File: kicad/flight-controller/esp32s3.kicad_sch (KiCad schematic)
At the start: 15 parts, among them J13 USB-C, SW1 TS-1088, SW2 TS-1088, U1 ESP32-S3-WROOM-1

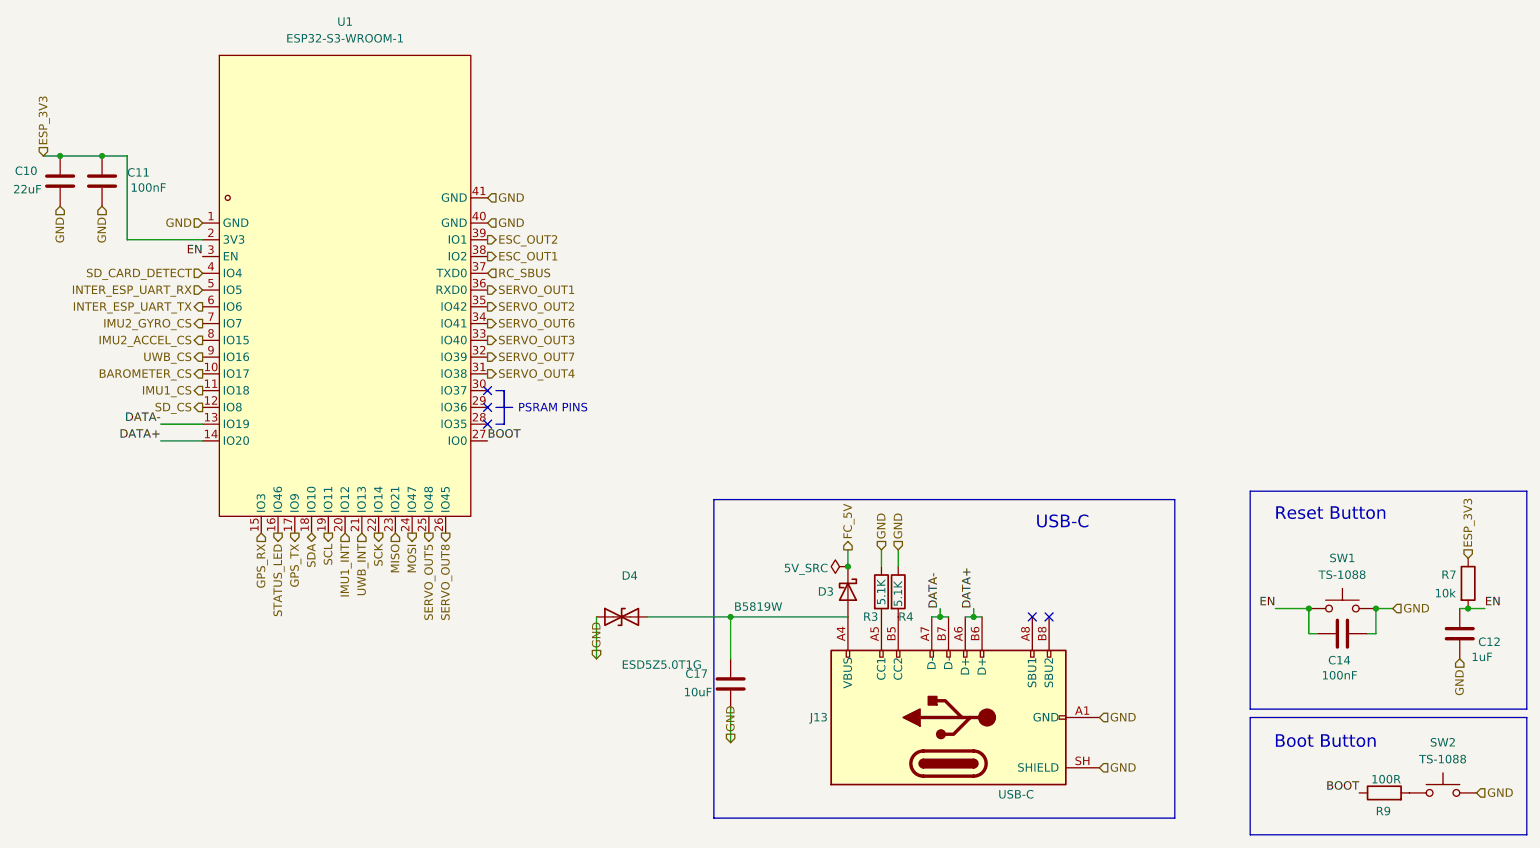
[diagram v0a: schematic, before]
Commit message: removed basestation code and v3.1 of fc pcb
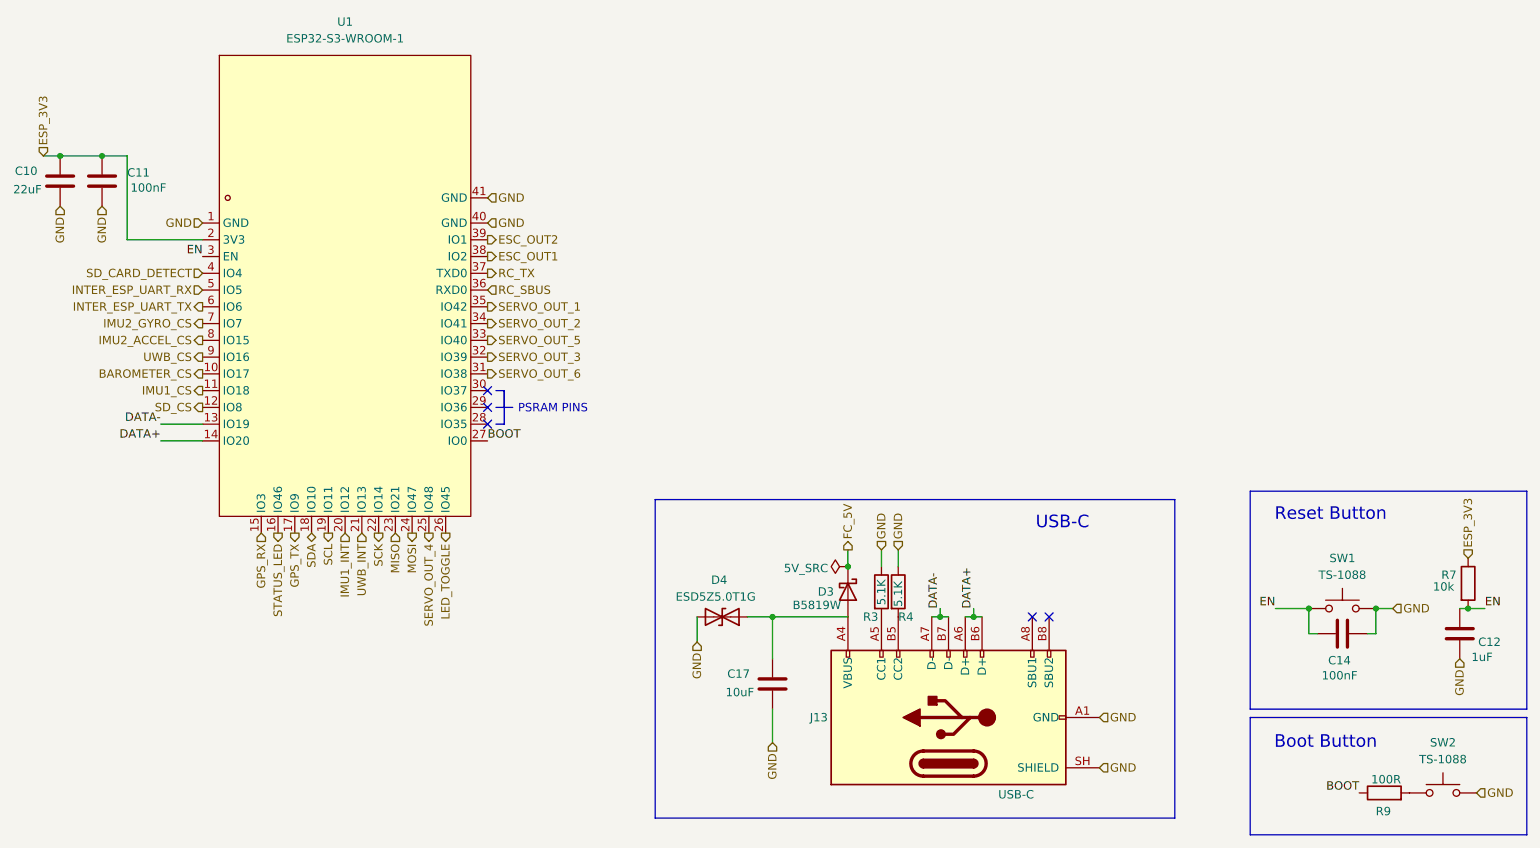
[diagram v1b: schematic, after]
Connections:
- net SERVO_OUT1 is gone; now on net RC_SBUS: U1.36 (RXD0)
- net GND: now also D4.2 (A2); no longer D4.1 (A1)
- net RC_SBUS: no longer U1.37 (TXD0)
- net at C17.1, D3.2 (A), J13.A4 (VBUS)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: now also D4.1 (A1); no longer D4.2 (A2)
- net SERVO_OUT2 renamed SERVO_OUT_1
- net SERVO_OUT3 renamed SERVO_OUT_5
- net SERVO_OUT4 renamed SERVO_OUT_6
- net SERVO_OUT5 renamed SERVO_OUT_4
- net SERVO_OUT6 renamed SERVO_OUT_2
- net SERVO_OUT7 renamed SERVO_OUT_3
- net SERVO_OUT8 renamed LED_TOGGLE
- new net RC_TX: U1.37 (TXD0)
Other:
- moved on the sheet: C17, D4
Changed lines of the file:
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@@
 	)
 	(rectangle
-		(start 152.4 100.33)
+		(start 143.51 100.33)
 		(end 222.25 148.59)
 		(stroke
@@
 	)
 	(junction
-		(at 154.94 118.11)
-		(diameter 0)
-		(color 0 0 0 0)
-	)
-	(junction
 		(at 172.72 110.49)
 		(diameter 0)
@@
 	)
 	(junction
+		(at 161.29 118.11)
+		(diameter 0)
+		(color 0 0 0 0)
+	)
+	(junction
 		(at 186.69 118.11)
 		(diameter 0)
@@
 	(wire
 		(pts
-			(xy 134.62 118.11) (xy 134.62 124.46)
+			(xy 149.86 118.11) (xy 149.86 121.92)
 		)
 		(stroke
@@
 	(wire
 		(pts
-			(xy 172.72 118.11) (xy 154.94 118.11)
+			(xy 172.72 118.11) (xy 161.29 118.11)
 		)
 		(stroke
@@
 	(wire
 		(pts
-			(xy 154.94 124.46) (xy 154.94 118.11)
+			(xy 161.29 124.46) (xy 161.29 118.11)
 		)
 		(stroke
@@
 	(wire
 		(pts
-			(xy 154.94 132.08) (xy 154.94 137.16)
+			(xy 161.29 132.08) (xy 161.29 137.16)
 		)
 		(stroke
@@
 	(wire
 		(pts
-			(xy 154.94 118.11) (xy 142.24 118.11)
+			(xy 157.48 118.11) (xy 161.29 118.11)
 		)
 		(stroke
@@
 			)
 			(justify left bottom)
+		)
+	)
+	(hierarchical_label "LED_TOGGLE"
+		(shape output)
+		(at 111.76 105.41 270)
+		(effects
+			(font
+				(size 1.27 1.27)
+			)
+			(justify right)
 		)
 	)
@@
 		)
 	)
-	(hierarchical_label "SERVO_OUT7"
-		(shape output)
-		(at 118.11 78.74 0)
-		(effects
-			(font
-				(size 1.27 1.27)
-			)
-			(justify left)
-		)
-	)
 	(hierarchical_label "UWB_CS"
 		(shape output)
@@
 	(hierarchical_label "RC_SBUS"
 		(shape input)
-		(at 118.11 66.04 0)
-		(effects
-			(font
-				(size 1.27 1.27)
-			)
-			(justify left)
-		)
-	)
-	(hierarchical_label "SERVO_OUT3"
-		(shape output)
-		(at 118.11 76.2 0)
+		(at 118.11 68.58 0)
 		(effects
 			(font
@@
 		)
 	)
+	(hierarchical_label "SERVO_OUT_2"
+		(shape output)
+		(at 118.11 73.66 0)
+		(effects
+			(font
+				(size 1.27 1.27)
+			)
+			(justify left)
+		)
+	)
 	(hierarchical_label "INTER_ESP_UART_RX"
 		(shape input)
@@
 		)
 	)
-	(hierarchical_label "SERVO_OUT4"
+	(hierarchical_label "SERVO_OUT_3"
 		(shape output)
-		(at 118.11 81.28 0)
+		(at 118.11 78.74 0)
 		(effects
 			(font
@@
 		)
 	)
-	(hierarchical_label "SERVO_OUT1"
+	(hierarchical_label "SERVO_OUT_4"
 		(shape output)
-		(at 118.11 68.58 0)
-		(effects
-			(font
-				(size 1.27 1.27)
-			)
-			(justify left)
+		(at 109.22 105.41 270)
+		(effects
+			(font
+				(size 1.27 1.27)
+			)
+			(justify right)
 		)
 	)
@@
 		)
 	)
-	(hierarchical_label "SERVO_OUT2"
-		(shape output)
-		(at 118.11 71.12 0)
-		(effects
-			(font
-				(size 1.27 1.27)
-			)
-			(justify left)
-		)
-	)
 	(hierarchical_label "INTER_ESP_UART_TX"
 		(shape output)
@@
 		)
 	)
+	(hierarchical_label "RC_TX"
+		(shape output)
+		(at 118.11 66.04 0)
+		(effects
+			(font
+				(size 1.27 1.27)
+			)
+			(justify left)
+		)
+	)
 	(hierarchical_label "GND"
 		(shape input)
@@
 	(hierarchical_label "GND"
 		(shape input)
-		(at 154.94 137.16 90)
-		(effects
-			(font
-				(size 1.27 1.27)
-			)
-			(justify left)
+		(at 161.29 137.16 270)
+		(effects
+			(font
+				(size 1.27 1.27)
+			)
+			(justify right)
 		)
 	)
@@
 		)
 	)
-	(hierarchical_label "SERVO_OUT6"
-		(shape output)
-		(at 118.11 73.66 0)
-		(effects
-			(font
-				(size 1.27 1.27)
-			)
-			(justify left)
-		)
-	)
 	(hierarchical_label "GPS_RX"
 		(shape input)
@@
 		)
 	)
-	(hierarchical_label "SERVO_OUT8"
-		(shape output)
-		(at 111.76 105.41 270)
-		(effects
-			(font
-				(size 1.27 1.27)
-			)
-			(justify right)
-		)
-	)
 	(hierarchical_label "ESP_3V3"
 		(shape input)
@@
 		)
 	)
-	(hierarchical_label "SERVO_OUT5"
+	(hierarchical_label "SERVO_OUT_5"
 		(shape output)
-		(at 109.22 105.41 270)
-		(effects
-			(font
-				(size 1.27 1.27)
-			)
-			(justify right)
+		(at 118.11 76.2 0)
+		(effects
+			(font
+				(size 1.27 1.27)
+			)
+			(justify left)
+		)
+	)
+	(hierarchical_label "SERVO_OUT_1"
+		(shape output)
+		(at 118.11 71.12 0)
+		(effects
+			(font
+				(size 1.27 1.27)
+			)
+			(justify left)
 		)
 	)
 	(hierarchical_label "GND"
 		(shape input)
-		(at 134.62 124.46 90)
-		(effects
-			(font
-				(size 1.27 1.27)
-			)
-			(justify left)
+		(at 149.86 121.92 270)
+		(effects
+			(font
+				(size 1.27 1.27)
+			)
+			(justify right)
 		)
 	)
@@
 		(shape output)
 		(at 118.11 63.5 0)
+		(effects
+			(font
+				(size 1.27 1.27)
+			)
+			(justify left)
+		)
+	)
+	(hierarchical_label "SERVO_OUT_6"
+		(shape output)
+		(at 118.11 81.28 0)
 		(effects
 			(font
@@
 	(symbol
 		(lib_id "Device:D_TVS")
-		(at 138.43 118.11 0)
+		(at 153.67 118.11 180)
 		(unit 1)
 		(body_style 1)
@@
 		(dnp no)
 		(property "Reference" "D4"
-			(at 138.43 111.89 0)
+			(at 154.432 112.522 0)
 			(show_name no)
 			(do_not_autoplace no)
@@
 		)
 		(property "Value" "ESD5Z5.0T1G"
-			(at 138.43 125.38 0)
+			(at 158.75 115.062 0)
 			(show_name no)
 			(do_not_autoplace no)
@@
 		)
 		(property "Footprint" "Diode_SMD:D_SOD-523"
-			(at 138.43 118.11 0)
+			(at 153.67 118.11 0)
 			(hide yes)
 			(show_name no)
@@
 		)
 		(property "Datasheet" "https://www.lcsc.com/datasheet/C82044.pdf"
-			(at 138.43 118.11 0)
+			(at 153.67 118.11 0)
 			(hide yes)
 			(show_name no)
@@
 		)
 		(property "Description" "TVS diode, onsemi, 5V standoff / 6.2V breakdown, unidirectional"
-			(at 138.43 118.11 0)
+			(at 153.67 118.11 0)
 			(hide yes)
 			(show_name no)
@@
 		)
 		(property "Notes" "USB VBUS ESD/surge protection (added in review)"
-			(at 138.43 118.11 0)
+			(at 153.67 118.11 0)
 			(hide yes)
 			(show_name no)
@@
 		)
 		(property "LCSC Part" "C82044"
-			(at 138.43 118.11 0)
+			(at 153.67 118.11 0)
 			(hide yes)
 			(show_name no)
@@
 		)
 		(property "Value" "10k"
-			(at 261.62 114.554 0)
+			(at 261.366 113.538 0)
 			(show_name no)
 			(do_not_autoplace no)
@@
 	(symbol
 		(lib_id "Device:C")
-		(at 154.94 128.27 0)
+		(at 161.29 128.27 0)
 		(unit 1)
 		(body_style 1)
@@
 		(dnp no)
 		(property "Reference" "C17"
-			(at 148.086 126.746 0)
+			(at 154.436 126.746 0)
 			(show_name no)
 			(do_not_autoplace no)
@@
 		)
 		(property "Value" "10uF"
-			(at 147.832 129.54 0)
+			(at 154.182 129.54 0)
 			(show_name no)
 			(do_not_autoplace no)
@@
 		)
 		(property "Footprint" "Capacitor_SMD:C_0805_2012Metric"
-			(at 154.94 128.27 0)
+			(at 161.29 128.27 0)
 			(hide yes)
 			(show_name no)
@@
 		)
 		(property "Datasheet" "https://www.lcsc.com/datasheet/C440198.pdf"
-			(at 154.94 128.27 0)
+			(at 161.29 128.27 0)
 			(hide yes)
 			(show_name no)
@@
 		)
 		(property "Description" "Unpolarized capacitor, Murata GRM21BR61H106KE43L, 50V X5R"
-			(at 154.94 128.27 0)
+			(at 161.29 128.27 0)
 			(hide yes)
 			(show_name no)
@@
 		)
 		(property "Notes" "USB VBUS bulk/decoupling cap (added in review)"
-			(at 154.94 128.27 0)
+			(at 161.29 128.27 0)
 			(hide yes)
 			(show_name no)
@@
 		)
 		(property "LCSC Part" "C440198"
-			(at 154.94 128.27 0)
+			(at 161.29 128.27 0)
 			(hide yes)
 			(show_name no)
@@
 		)
 		(property "Value" "B5819W"
-			(at 155.448 116.586 90)
-			(show_name no)
-			(do_not_autoplace no)
+			(at 164.338 116.332 90)
+			(show_name no)
+			(do_not_autoplace no)

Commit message: pcb progress
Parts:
- added D8, D9: ESD5Z5.0T1G, Diode_SMD:D_SOD-523, symbol Device:D_TVS
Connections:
- net DATA+: now also D8.1 (A1)
- net DATA-: now also D9.1 (A1)
- net GND: now also D8.2 (A2), D9.2 (A2)

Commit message: Kicad FC v3.1 complete, Mission Controller and UWB boards v1 complete, firmware v2 complete!
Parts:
- removed D8, D9: ESD5Z5.0T1G, Diode_SMD:D_SOD-523, symbol Device:D_TVS
- added U5: USBLC6-2SC6, Package_TO_SOT_SMD:SOT-23-6, symbol Power_Protection:USBLC6-2SC6
- U1: LCSC Part C2913202 -> C2913205; MPN ESP32-S3-WROOM-1-N16R8 -> ESP32-S3-WROOM-1-N16R2
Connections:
- net DATA+: now also U5.1 (I/O1), U5.6 (I/O1)
- net DATA-: now also U5.3 (I/O2), U5.4 (I/O2)
- net GND: now also U5.2 (GND)
- net SD_CS: now also U1.30 (IO37); no longer U1.12 (IO8)
- net USB_VBUS: now reaches C17.1, D3.2 (A), D4.1 (A1), J13.A4 (VBUS), J13.A9 (VBUS), J13.B4 (VBUS), J13.B9 (VBUS)
- net USB_VBUS: now also U5.5 (VBUS)
- net SD_SCK: now reaches U1.28 (IO35)
- net SD_MOSI: now reaches U1.29 (IO36)
- new net SD_MISO: U1.12 (IO8)
- no-connect marks 5 -> 2
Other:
- note removed: "PSRAM PINS"
